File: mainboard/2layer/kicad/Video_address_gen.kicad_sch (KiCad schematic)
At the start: 15 parts, among them U12 74LS193, U13 74LS193, U14 74LS11, U15 74LS74, U16 74LS00, U19 74LS08, U32 74LS193, U33 74LS193, U34 74LS20, U35 74LS86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

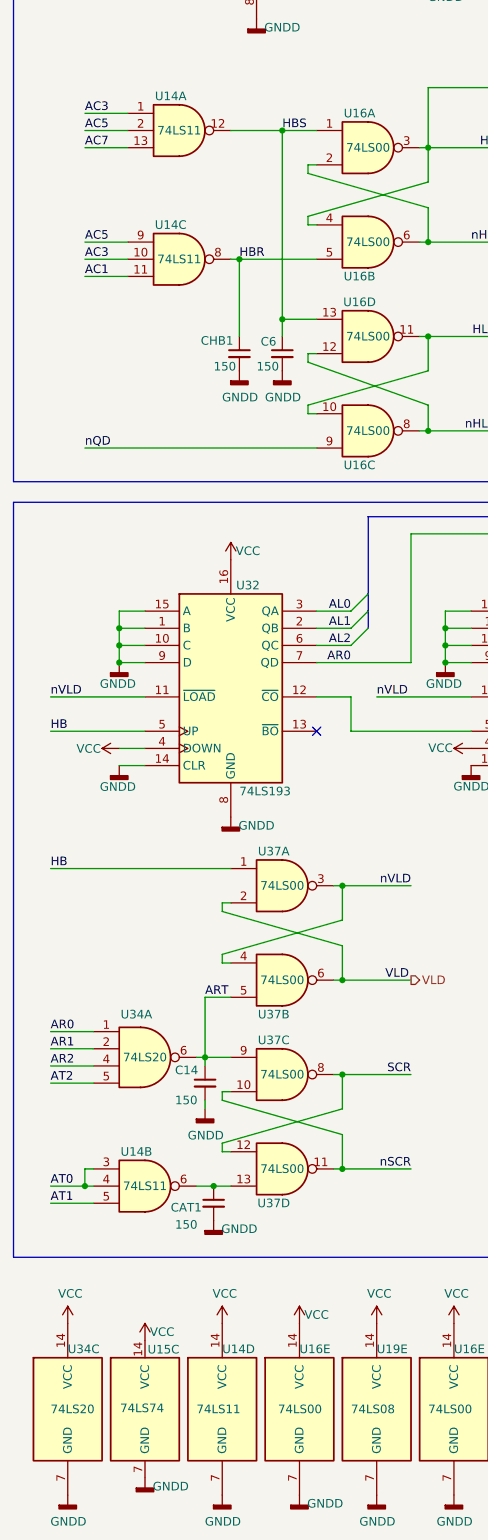
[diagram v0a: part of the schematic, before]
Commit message: update U14 symbol name to 74LS10
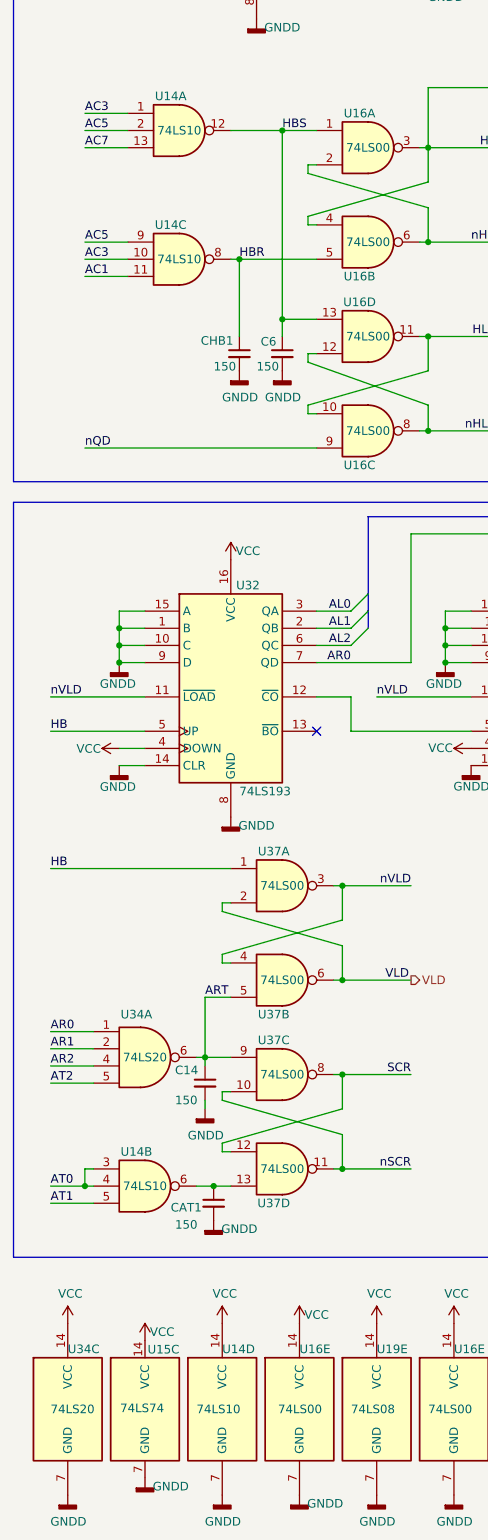
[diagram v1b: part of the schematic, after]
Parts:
- U14: value 74LS11 -> 74LS10
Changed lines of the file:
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@@
       (effects (font (size 1.27 1.27)))
     )
-    (property "Value" "74LS11" (at 39.37 93.98 0)
+    (property "Value" "74LS10" (at 39.37 93.98 0)
       (effects (font (size 1.27 1.27)))
     )
@@
       (effects (font (size 1.27 1.27)))
     )
-    (property "Value" "74LS11" (at 39.37 74.93 0)
+    (property "Value" "74LS10" (at 39.37 74.93 0)
       (effects (font (size 1.27 1.27)))
     )
@@
       (effects (font (size 1.27 1.27)))
     )
-    (property "Value" "74LS11" (at 34.29 231.14 0)
+    (property "Value" "74LS10" (at 34.29 231.14 0)
       (effects (font (size 1.27 1.27)))
     )
@@
       (effects (font (size 1.27 1.27)) (justify left))
     )
-    (property "Value" "74LS11" (at 41.91 264.16 0)
+    (property "Value" "74LS10" (at 41.91 264.16 0)
       (effects (font (size 1.27 1.27)) (justify left))
     )
